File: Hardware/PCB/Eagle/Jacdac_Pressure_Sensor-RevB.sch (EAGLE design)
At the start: 29 parts, among them IC1 LPS33HWTR, IC2 STM32G030F6P6, J1 JD, J2 PWR, J3 GND, J4 GND, J5 HACK-CONNECT-5, U1 XC6206

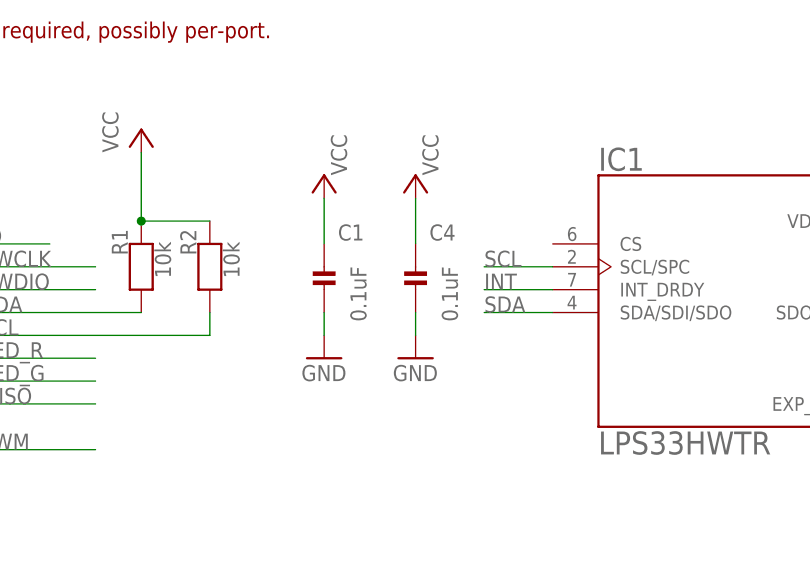
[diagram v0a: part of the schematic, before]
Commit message: Updated components value
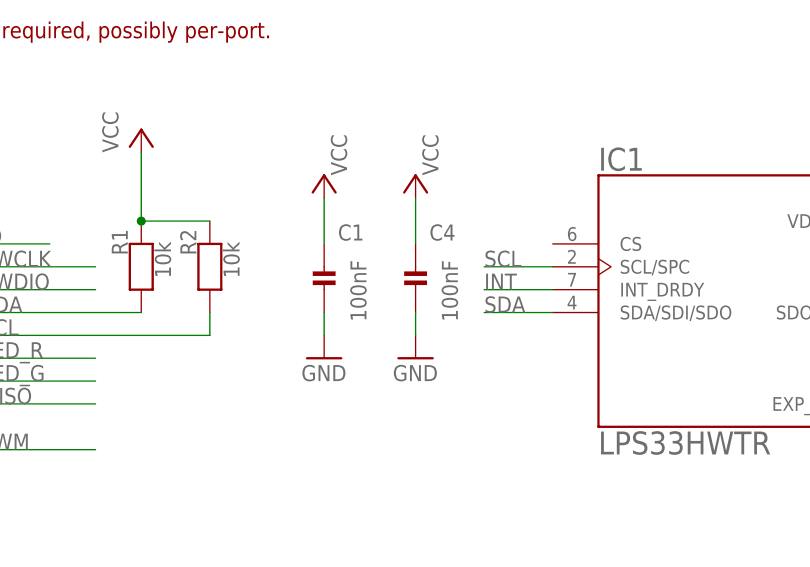
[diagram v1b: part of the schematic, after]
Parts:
- C1, C4: value 0.1uF -> 100nF
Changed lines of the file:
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@@
 <part name="R1" library="milador_SMD" library_urn="urn:adsk.eagle:library:27847482" deviceset="RESISTOR-" device="0402" package3d_urn="urn:adsk.eagle:package:36491935/2" value="10k"/>
 <part name="R2" library="milador_SMD" library_urn="urn:adsk.eagle:library:27847482" deviceset="RESISTOR-" device="0402" package3d_urn="urn:adsk.eagle:package:36491935/2" value="10k"/>
-<part name="C1" library="milador_SMD" library_urn="urn:adsk.eagle:library:27847482" deviceset="CAP_CERAMIC-" device="0402" package3d_urn="urn:adsk.eagle:package:36491935/2" value="0.1uF"/>
+<part name="C1" library="milador_SMD" library_urn="urn:adsk.eagle:library:27847482" deviceset="CAP_CERAMIC-" device="0402" package3d_urn="urn:adsk.eagle:package:36491935/2" value="100nF"/>
 <part name="GND6" library="supply1" library_urn="urn:adsk.eagle:library:371" deviceset="GND" device=""/>
 <part name="P+11" library="milador" library_urn="urn:adsk.eagle:library:12595918" deviceset="VCC" device=""/>
-<part name="C4" library="milador_SMD" library_urn="urn:adsk.eagle:library:27847482" deviceset="CAP_CERAMIC-" device="0402" package3d_urn="urn:adsk.eagle:package:36491935/2" value="0.1uF"/>
+<part name="C4" library="milador_SMD" library_urn="urn:adsk.eagle:library:27847482" deviceset="CAP_CERAMIC-" device="0402" package3d_urn="urn:adsk.eagle:package:36491935/2" value="100nF"/>
 <part name="GND9" library="supply1" library_urn="urn:adsk.eagle:library:371" deviceset="GND" device=""/>
 <part name="P+12" library="milador" library_urn="urn:adsk.eagle:library:12595918" deviceset="VCC" device=""/>
